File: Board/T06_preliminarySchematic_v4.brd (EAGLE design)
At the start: 59.4 x 80 mm, 57 parts, among them M1 SSW-102-02-S-S, M2 SSW-102-02-S-S, Q3 2n3904, U1 ATMEGA328P_PDIP, X1 SSW-105-02-S-S, X2 SSW-102-02-S-S

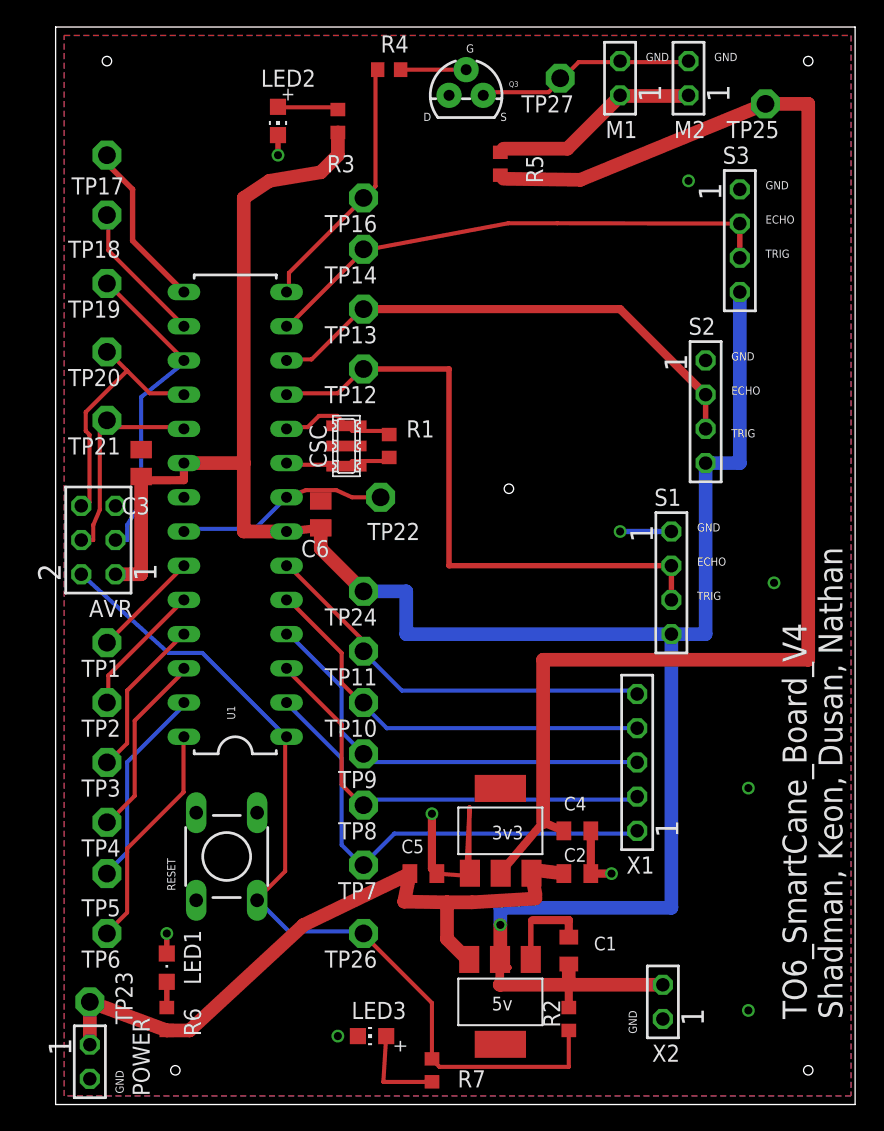
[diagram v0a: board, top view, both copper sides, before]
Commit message: Nade some visual changes to TNAMES on the board so that they are not overlapping. Added pin Names to AVR ISP
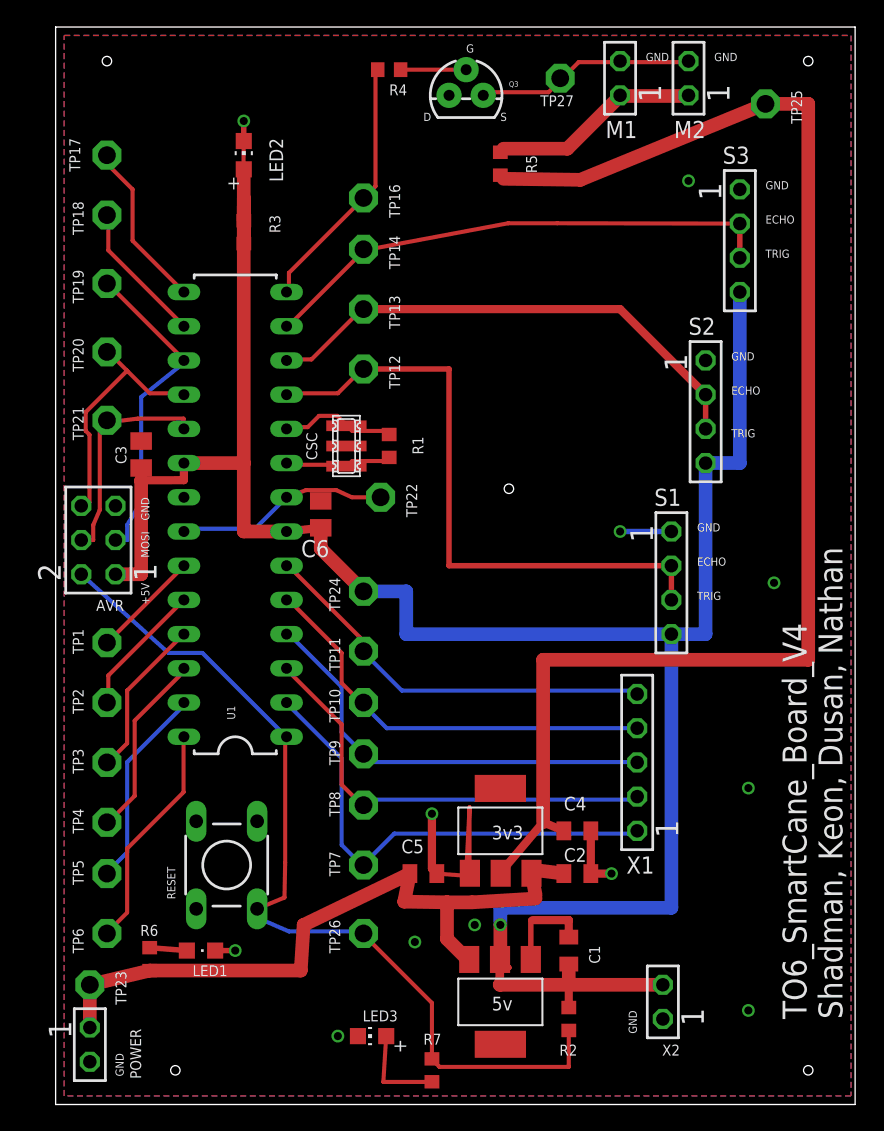
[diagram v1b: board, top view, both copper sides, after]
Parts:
- moved R3 10.8 mm to (14.0, 64.8)
- moved R6 4.62 mm to (6.99, 10.8)
- moved LED2 3.59 mm to (14.0, 70.5), turned to 0 degrees
- moved LED1 2.84 mm to (10.8, 11.4), turned to 270 degrees
- moved POWER 1.27 mm to (2.54, 4.45)
- moved TP23 1.27 mm to (2.54, 8.89)
- moved C3 0.63 mm to (6.35, 48.3)
- moved RESET 0.63 mm to (12.7, 17.8)
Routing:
- net +5V: track 182.4 -> 175.4 mm
- net GND: track 55.3 -> 58.0 mm, vias 10 -> 12
- net RESET: track 66.5 -> 67.5 mm
- net N$7: track 1.91 -> 2.77 mm
- net N$8: track 4.61 -> 3.81 mm
- net SCK: track 16.6 -> 17.2 mm
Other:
- board text added: "+5V"
- board text added: "MOSI"

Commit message: minor adjustments
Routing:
- net +5V: track 175.4 -> 169.2 mm
- net GND: track 58.0 -> 56.0 mm
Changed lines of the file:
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@@
 <?xml version="1.0" encoding="utf-8"?>
 <!DOCTYPE eagle SYSTEM "eagle.dtd">
-<eagle version="7.3.0">
+<eagle version="7.4.0">
 <drawing>
 <settings>
@@
 <layer number="42" name="bRestrict" color="1" fill="10" visible="yes" active="yes"/>
 <layer number="43" name="vRestrict" color="2" fill="10" visible="yes" active="yes"/>
-<layer number="44" name="Drills" color="7" fill="1" visible="no" active="yes"/>
+<layer number="44" name="Drills" color="7" fill="1" visible="yes" active="yes"/>
 <layer number="45" name="Holes" color="7" fill="1" visible="yes" active="yes"/>
 <layer number="46" name="Milling" color="3" fill="1" visible="yes" active="yes"/>
@@
 <wire x1="21.59" y1="48.895" x2="20.3454" y2="48.895" width="0.3048" layer="1"/>
 <wire x1="6.4008" y1="48.7426" x2="6.35" y2="49.26" width="0.3048" layer="1"/>
-<wire x1="13.9446" y1="69.5452" x2="13.97" y2="71.535" width="0.3048" layer="1"/>
 <wire x1="23.8506" y1="45.085" x2="24.384" y2="45.1866" width="0.3048" layer="1"/>
 <wire x1="30.734" y1="22.0726" x2="30.734" y2="17.3228" width="0.3048" layer="1"/>
@@
 <wire x1="6.35" y1="46.3296" x2="6.35" y2="39.37" width="1.016" layer="1"/>
 <wire x1="6.35" y1="39.37" x2="4.445" y2="39.37" width="1.016" layer="1"/>
-<wire x1="13.97" y1="47.625" x2="13.97" y2="67.31" width="1.016" layer="1"/>
-<wire x1="13.97" y1="66.675" x2="13.97" y2="63.92" width="1.016" layer="1"/>
-<wire x1="13.97" y1="67.31" x2="13.97" y2="66.675" width="0" layer="19" extent="1-1"/>
-<wire x1="6.35" y1="46.355" x2="6.35" y2="46.3296" width="0" layer="19" extent="1-1"/>
+<wire x1="13.97" y1="47.625" x2="13.97" y2="62.23" width="1.016" layer="1"/>
+<wire x1="13.97" y1="62.23" x2="13.97" y2="62.865" width="1.016" layer="1"/>
+<wire x1="13.97" y1="62.865" x2="13.97" y2="63.92" width="1.016" layer="1"/>
+<wire x1="6.35" y1="46.3296" x2="6.35" y2="46.355" width="0" layer="19" extent="1-1"/>
 </signal>
 <signal name="N$5">
